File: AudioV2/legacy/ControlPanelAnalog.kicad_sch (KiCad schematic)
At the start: 39 parts, among them SW401 DEST sense (3PDT 3rd pole), SW402 PWR SW, U401 Pico 2 / RP2350, U402 PT2314-D, U403 BP5293-50 +5V

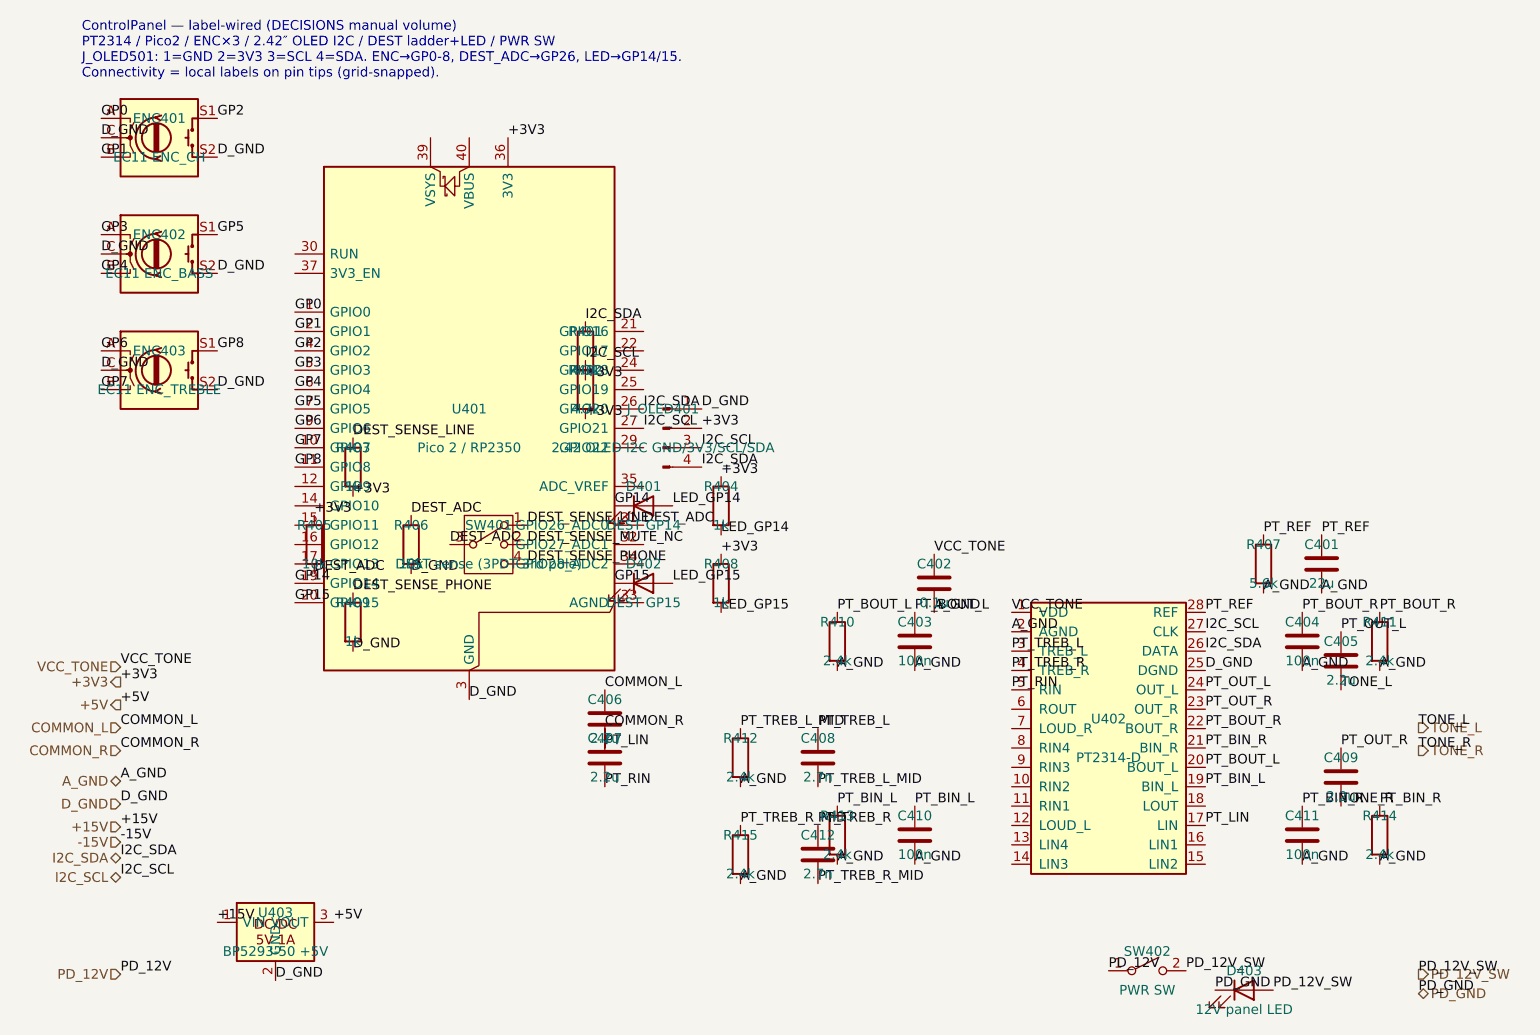
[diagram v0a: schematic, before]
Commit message: AudioV2: B4'-1/B4'-2 完了。ControlPanel を解体し、シートは4枚になった
B4'-1（UI と I2C マスタを計測基板へ / D27）:
- MeasureControl に MCP23017(U1610, 0x22)＋100nF、ENC1601-1603、DEST LED×2＋1k、
  OLED、I2C プルアップ 4.7k×2、DEST センスラダー（SW1601＋抵抗4本）を追加
- 計測 Pico の空きピンへ直付け: GPIO20/21 = I2C_SDA/SCL、GPIO26(ADC0) = DEST_ADC
- **系の 3V3 は A1602.36（計測 Pico の 3V3_OUT）から**。+3V3_A（LT1763）は
  PCM1804・水晶・監視ICの清浄レールなので触っていない（D27）
- 階層ピンに I2C_SDA / I2C_SCL / 3V3 / D_GND を追加

B4'-2（PT2314 と +5V を母板へ、ControlPanel 廃止）:
- 残り23部品（PT2314＋周辺20点・BP5293-50・パネル PWR SW・12V LED）を母板へ統合
- VCC_TONE と PD_12V は作る側と使う側の両方が母板に収まったので階層ピンから外した
- 母板の階層ピンは 21 本。TONE_L/R と +5V は input -> output へ（母板が作る側になった）
- 母板の用紙を A3 -> A2 へ

検証:
- 部品 370 個すべてユニーク。シートは MotherBoard / MeasureControl /
  AmpBankSwitch / AmpBankRelay の4枚（ControlPanel は消滅、U401 も消えた）
- /3V3 の駆動は A1602.36、/+5V の駆動は U403.3（BP5293、母板）
- /VCC_TONE と /PD_12V はルートから消えて母板内部のネットになった
- **ERC 49 -> 29**。残る multiple_net_names 1件は 3V3/PICO_3V3 の意図的な別名

途中で3件やらかして直した:
1. **既存の配線の上に新部品を重ねた。** MeasureControl の使用範囲を要素の
   アンカーだけで測って y<=233.7 と誤ったが、**ワイヤの端点まで入れると y=315**
   だった。空きを測るときはワイヤの端点も入れること
2. **親で同じネットに2つ名前が付いた。** 元の7ピンはユーザーが (234.95,y) の
   ラベル＋ワイヤで結線済みなのに、ピン位置にもラベルを重ねたため。
   増えた4本にだけ置くようにした
3. **計測 Pico の空きピンに残っていた no_connect** を外さずにラベルを乗せて
   no_connect_connected になった

Co-Authored-By: Claude Opus 5 <noreply@anthropic.com>
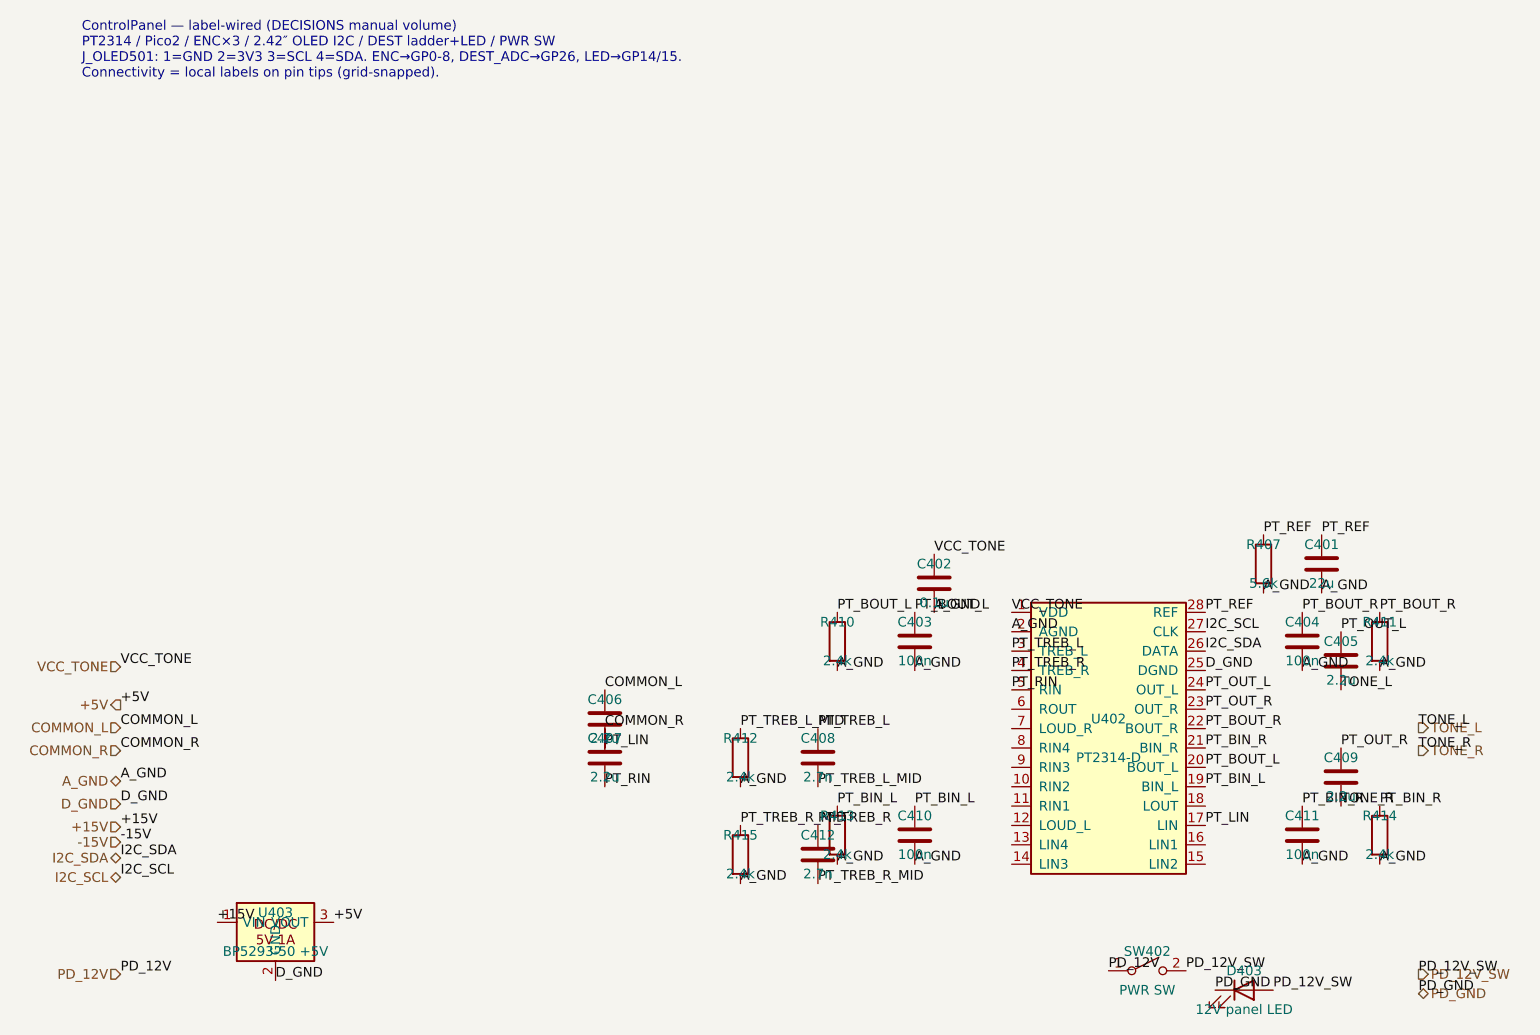
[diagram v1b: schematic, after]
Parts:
- removed D401: DEST GP14, symbol Device:LED
- removed D402: DEST GP15, symbol Device:LED
- removed ENC401: EC11 ENC_CH, symbol Device:RotaryEncoder_Switch
- removed ENC402: EC11 ENC_BASS, symbol Device:RotaryEncoder_Switch
- removed ENC403: EC11 ENC_TREBLE, symbol Device:RotaryEncoder_Switch
- removed J_OLED401: 2.42 OLED I2C GND/3V3/SCL/SDA, symbol Connector:Conn_01x04_Pin
- removed R401, R402: 4.7k, symbol Device:R
- removed R403, R404, R408, R409: 1k, symbol Device:R
- removed R405, R406: 10k, symbol Device:R
- removed SW401: DEST sense (3PDT 3rd pole), symbol Switch:SW_SP3T
- removed U401: Pico 2 / RP2350, symbol MCU_Module:RaspberryPi_Pico

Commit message: AudioV2: コイル電源が通電しない状態だったのを是正（+5V_COIL の閉路を成立させた）
## 見つけた不具合

母板の `U403`（BP5293-50、娘基板のコイル電源）が
  入力 `/+15V`（二次・A_GND 基準）/ 帰路 `/D_GND`
という組み合わせだった。NetTie でグラウンドの連結成分を辿ると

  成分1: /A_GND + /ADC_GND          ← 二次
  成分4: /D_GND + /GND_COIL + /PD_GND ← 一次・コイル

で **A_GND と D_GND は繋がっていない**（A6/D28「NetTie は足さない」）。
つまり `U403` の帰路が電源側の成分へ戻れず、**`+5V` レールは通電しない**。

さらに母板側だけネット名が `+5V` で、娘基板と親が宣言している `+5V_COIL` と
食い違い、合流して `/+5V` に潰れていた。`build_daughter.py` の `PARENT_NET` に
`"+5V_COIL": "+5V"` という橋渡しが入っており、コメントも「母板側のネット名が別」
と書いてあった（回避策であって設計意図ではない）。

## 経緯（追いかけた結果）

- v1 の同じ BP5293（`U501`）は**入力が未接続**で、5 V は Pico の USB/VSYS から
  取っていた（`5V_+` に `A501.39(VSYS)` が繋がっている）。制御系は専用 `CTRL_GND`
- AudioV2 の `ControlPanel` で入力に `+12V`（`-12V` と対の**アナログ二次**レール。
  `PD_12V` とは別名）を繋いだのが発端。`ca0af51` の `+12V→+15V` 一括改名の
  産物ではなく、それ以前から
- §1 が書いていた「`A_GND`/`D_GND` の NetTie は ControlPanel 側1点」は、
  旧 ControlPanel を確認したら **NetTie が1個も無く、意図の記述だけ**だった
- つまり BP5293 をコイル電源として使う構成は v1 でも AudioV2 でも一度も通電していない

## 直したこと（部品は増やしていない）

素材 `legacy/ControlPanelAnalog.kicad_sch` の `U403` まわり:

  pin1 VIN   +15V   -> PD_12V_SW    帰路と同じ成分から取る（U1607 と同じ形）
  pin2 GND   D_GND  -> GND_COIL     NT101 を唯一の結合点に保つ
  pin3 VOUT  +5V    -> +5V_COIL     娘基板・親の宣言と名前を一致させる
  階層ラベル +5V    -> +5V_COIL     同座標に平文と階層の両方があり、最初は平文だけ直して
                                    母板側が sheet-local に取り残された

生成器側:
- `build_motherboard.py` の `MOTHER_PINS_R` と `SLOT_PWR_NETS[5]` を `+5V_COIL` へ
- `build_daughter.py` の `PARENT_NET` の橋渡しを恒等に（名前が揃ったので不要）

**レギュレータを娘基板へ移す案は採らなかった。** 移す動機（速い電流をコネクタに
渡さない）は既に娘基板の `C321`(100µF)/`C322`(100nF) のローカルバイパスで
達成されており、移すとヘッダに 12 V が必要になって D18/D20 のピン割当変更と
リレー娘基板ごとのレギュレータ追加が発生する。得るものはほぼ無い。

## 検証

- check_sexpr 13/0、sch_import --roundtrip 全6ファイル OK
- 再生成は CLAUDE.md の規則どおり build_daughter -> build_motherboard を2巡
- **ERC 29 件・内訳も完全一致**
- 部品 369（NetTie 3個含む）/ ネット 327 — どちらも変化なし
- `/+5V_COIL` が**18ノードの単一ネット**に統合（U403.3 + 母板スロット2 +
  娘基板ヘッダ + C321/C322 + コイル5個 + ドライバ2個）。旧 `/+5V` は消滅
- **`/A_GND` <-> `/D_GND` = False**（絶縁維持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
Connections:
- net +15V: no longer U403.1 (VIN)
- net D_GND: no longer U403.2 (GND)
- net PD_12V_SW: now also U403.1 (VIN)
- net +5V renamed +5V_COIL
- new net GND_COIL: U403.2 (GND)
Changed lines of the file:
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@@
 		)
 	)
-	(label "+5V"
+	(label "+5V_COIL"
 		(at 58.42 143.51 0)
 		(effects
@@
 		)
 	)
-	(label "D_GND"
+	(label "GND_COIL"
 		(at 50.8 151.13 0)
 		(effects
@@
 		)
 	)
-	(label "+15V"
+	(label "PD_12V_SW"
 		(at 43.18 143.51 0)
 		(effects
@@
 		)
 	)
-	(label "+5V"
+	(label "+5V_COIL"
 		(at 30.48 115 0)
 		(effects
@@
 		)
 	)
-	(hierarchical_label "+5V"
+	(hierarchical_label "+5V_COIL"
 		(shape output)
 		(at 30.48 115 180)

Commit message: AudioV2: PPTC 2個を実装（U403 / U1607 の手前）。U202 は幾何的に入らず未実装
## 実装したもの

  F202  PPTC 0.35A hold  legacy/PowerModule に置き  PD_12V_SW -> PD_12V_COIL -> U403
  F1602 PPTC 0.5A hold   MeasureControl の縦配線を分割 PD_12V_SW -> PD_12V_MEAS -> U1607

F202 は `legacy/ControlPanelAnalog` ではなく `legacy/PowerModule` に置いた。
統合後は同じシートになるのでネットは繋がるうえ、PowerModule には `Device:Fuse` が
既に埋め込まれており lib_symbols の追加が不要。電源保護が電源シートに載るのも筋が通る。
`ControlPanelAnalog` 側は `U403` の入力ラベルを `PD_12V_COIL` へ改名しただけ。

`PD_12V_COIL` / `PD_12V_MEAS` に PWR_FLAG（#FLG0202 / #FLG1602）を追加。
PPTC は受動素子なので、これが無いと KiCad が VIN を「電源が駆動していない」と判定して
ERC が 31 件に増える（実際に増えたので足した）。

## U202 前は未実装（幾何的な理由）

`+15V` の T 点 (144.78,77.47) から `U202.1` (147.32,77.47) への配線が **2.54 mm の
スタブ**で、7.62 mm の素子が入らない。T 点の上流に入れると別の枝も一緒に保護して
しまうので不可。`U202` を数 mm ずらすか引き回しを変える必要があり、それは GUI で
見ながらやる作業。30 mA の枝なので優先度は低い。DECISIONS §8 に⚠として記録した。

## ⚠ 前回の判定を訂正した（DECISIONS の記述も直した）

8c1c558 で「U403 の帰路が二次側へ戻れず通電しない」と書いたが**誤り**。
DECISIONS の A6 が結合チェーンを図示していた:

  A_GND ─NT1601─ ADC_GND ─U1604─ PD_GND ─NT1602─ MC/D_GND
                          (MBC2596 は非絶縁バック。IN- と OUT- は同一ノード)

私の解析は NetTie だけを辿って、この非絶縁バックの内部ボンドを見落としていた。
**帰路は存在した。** 問題は通電の有無ではなく経路で、リレーのパルス電流が結合
チェーン全体、つまり **ADC のアナログ星点を通って**いた。是正の価値は変わらないが、
機構の説明が間違っていたので DECISIONS の D18 実装表を訂正した。

## もう1つ見つけた（未判断）

**`U1604`（`MBC2596-01`、計測系の降圧 DC-DC）はヒューズの外。** `PD_12V_SW` に
直付けで上流は `F1601` のみ。「各コンバータの手前」を徹底するならここにも要る。
DECISIONS §8 に⚠として記録。

## 検証

- check_sexpr 13/0、sch_import --roundtrip 全6ファイル OK
- 再生成は build_daughter -> build_motherboard を2巡（CLAUDE.md の規則）
- **ERC 29 件・内訳も完全一致**（PWR_FLAG 追加前は 31 件）
- 部品 369 -> **371**（F202 / F1602。PWR_FLAG は netlist の components に出ない）
  重複 0 / 未注釈 0
- 結線を netlist で確認:
    /MotherBoard/PD_12V_COIL    = F202.2 + U403.1
    /MeasureControl/PD_12V_MEAS = F1602.2 + U1607.1
    /PD_12V_SW                  = F201.1 / F202.1 / F1602.1 + LED + SW + U1604 + caps
- gen_parts_bom --check rc=0。BOM 366 -> 368

Co-Authored-By: Claude Opus 5 <noreply@anthropic.com>
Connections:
- net PD_12V_SW: no longer U403.1 (VIN)
- new net PD_12V_COIL: U403.1 (VIN)
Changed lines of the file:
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@@
 		)
 	)
-	(label "PD_12V_SW"
+	(label "PD_12V_COIL"
 		(at 43.18 143.51 0)
 		(effects
